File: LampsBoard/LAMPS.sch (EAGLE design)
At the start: 48 parts, among them IC1 LM358N, IC2 LM358N, IC3 5V, IC4 78L12Z, IC5 78L12Z, Q1 TIP120

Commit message: More work...
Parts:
- removed IC2: LM358N, linear:LM358N
- removed X, Y: (no value), pinhead:PINHD-1X1
- added 12V-AUX: (no value), SparkFun:M02PTH
- added 3.3V, 5V, VCC: (no value), adafruit:PINHD-1X1
- added ADCH1: 8-15, pinhead:PINHD-1X8
- added AUX1, COMM: 14-21, pinhead:PINHD-1X8
- added F3: MFR500, RepRapjr:PTCFUSE
- added IC6: UA741P, linear:UA741P
- added JP7: 22-37, pinhead:PINHD-2X8
- added R4, R5, R6, R7: 5K, SparkFun:RESISTORAXIAL-0.3
- added S2: (no value), switch-omron:31-XX
- added X-GALVO, Y-GALVO: 22-23-2031, con-molex:22-23-2031
- added X1: MSTBA2, con-phoenix-508:MSTBA2
- IC1: value LM358N -> UA741P; device linear:LM358N -> linear:UA741P
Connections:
- new net +12V: 12V-AUX.1, C10.1, C12.1, C13.1, F3.1, IC3.IN, IC4.VI, IC5.VI, Z-AXIS.VMOT
- new net N$27: IC6.V-, X-GALVO-3.S
- new net N$28: IC6.V+, X-GALVO-1.S
- new net N$29: COMM.2, COMMUNICATION.2
- new net N$30: R7.1
- new net N$31: IC1.OUT, R6.2, Y-GALVO-2.S
- new net N$32: IC1.V-, Y-GALVO-3.S
- new net N$33: IC1.V+, Y-GALVO-1.S
- new net N$34: IC1.+IN
- new net N$35: COMM.3, COMMUNICATION.3
- new net N$36: F3.2, X1-1.1
- new net N$37: COMM.4, COMMUNICATION.4
- new net N$38: COMM.5
- new net N$39: COMM.6, COMMUNICATION.6
- new net N$40: COMM.7, COMMUNICATION.7
- new net N$41: COMM.8, COMMUNICATION.8
- new net N$42: ADCH.1, ADCH1.1
- new net N$43: ADCH1.2
- new net N$44: ADCH.3, ADCH1.3
- new net N$45: ADCH.4, ADCH1.4
- new net N$46: ADCH.5, ADCH1.5
- new net N$47: ADCH.6, ADCH1.6
- new net N$48: ADCH.7, ADCH1.7
- new net N$49: ADCH.8, ADCH1.8
- new net N$50: JP1.15, JP7.15
- new net N$51: JP1.16, JP7.16
- new net N$52: JP1.13, JP7.13
- new net N$53: JP1.14, JP7.14
- new net N$54: JP1.11, JP7.11
- new net N$55: JP1.12, JP7.12
- new net N$56: JP1.9, JP7.9
- new net N$57: JP1.10, JP7.10
- new net N$58: JP1.7, JP7.7
- new net N$59: JP1.8, JP7.8
- new net N$60: JP1.5, JP7.5
- new net N$61: JP1.6, JP7.6
- new net N$62: JP1.3, JP7.3
- new net N$63: JP1.4, JP7.4
- new net N$64: JP1.1, JP7.1
- new net N$65: JP1.2, JP7.2
- new net N$74: AUX1.1, PWML.1
- new net N$75: AUX1.2, PWML.2
- new net N$76: AUX1.3, PWML.3
- new net N$77: AUX1.4, PWML.4
- new net N$78: AUX1.5, PWML.5
- new net N$79: AUX1.6, PWML.6
- new net N$80: AUX1.7, PWML.7
- new net RESET: POWER.1, S2.S
- net GND: now also 12V-AUX.2, AUX1.8, IC1.-IN, IC6.-IN, POWER.4, POWER.5, R4.1, R5.2, R6.1, R7.2, S2.P, X1-2.1
- net N$10: now also 5V.1, POWER.3; no longer IC2A.-IN, IC2A.OUT, Y.1
- net N$5: now also IC6.+IN; no longer IC1A.+IN
- net N$6: now also R5.1
- net N$7: now also IC6.OUT, R4.2, X-GALVO-2.S; no longer IC1A.-IN, IC1A.OUT, X.1
- net N$8: now also 3.3V.1, POWER.2; no longer AD420ARZ1.17, IC2A.+IN
- net N$9: now also COMM.1, COMMUNICATION.1; no longer AD420ARZ1.14, AD420ARZ1.15
- net VCC: now also VCC.1; no longer C10.1, C12.1, C13.1, IC3.IN, IC4.VI, IC5.VI, Z-AXIS.VMOT

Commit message: Switching AD420 Chip mount
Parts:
- removed AD420ARZ, AD420ARZ1: (no value), special:SW_DIP-12
- added AUX2: 14-21, pinhead:PINHD-1X8
- added B2, B3: (no value), SparkFun:M02PTH
- added IC2, IC7: AD420ARZ, ic-package:DIL24-3
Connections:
- new net D40: B3.1, JP2.14
- new net D42: B2.1, JP2.12
- new net N$66: AUX2.1, JP2.15
- new net N$67: AUX2.2, JP2.13
- new net N$68: AUX2.3, JP2.11
- new net N$69: AUX2.4, JP2.9
- new net N$70: AUX2.5, JP2.7
- new net N$71: AUX2.6, JP2.5
- new net N$72: AUX2.7, JP2.3
- new net N$73: AUX2.8, JP2.1
- net D10: now also IC7.9; no longer AD420ARZ.9
- net D11: now also IC2.7; no longer AD420ARZ1.7
- net D12: now also IC2.8; no longer AD420ARZ1.8
- net D7: now also IC2.9; no longer AD420ARZ1.9
- net D8: now also IC7.7; no longer AD420ARZ.7
- net D9: now also IC7.8; no longer AD420ARZ.8
- net GND: now also B2.2, B3.2, IC2.11, IC2.4, IC2.5, IC2.6, IC7.11, IC7.4, IC7.5, IC7.6; no longer AD420ARZ.11, AD420ARZ.4, AD420ARZ.5, AD420ARZ.6, AD420ARZ1.11, AD420ARZ1.4, AD420ARZ1.5, AD420ARZ1.6
- net N$1: now also IC2.21; no longer AD420ARZ1.21
- net N$18: now also IC7.23; no longer AD420ARZ.23
- net N$19: now also IC7.2; no longer AD420ARZ.2
- net N$2: now also IC2.20; no longer AD420ARZ1.20
- net N$24: now also IC2.2; no longer AD420ARZ1.2
- net N$25: now also IC2.23; no longer AD420ARZ1.23
- net N$3: now also IC7.21; no longer AD420ARZ.21
- net N$30: now also IC2.14, IC2.15
- net N$34: now also IC2.17
- net N$4: now also IC7.20; no longer AD420ARZ.20
- net N$5: now also IC7.17; no longer AD420ARZ.17
- net N$6: now also IC7.14, IC7.15; no longer AD420ARZ.14, AD420ARZ.15

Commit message: movin
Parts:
- removed JP7: 22-37, pinhead:PINHD-2X8
- IC2, IC7: value AD420ARZ -> (none); device ic-package:DIL24-3 -> ic-package:DIL24-6
- renumbered X1 to 12V
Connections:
- removed net N$50: JP1.15, JP7.15
- removed net N$51: JP1.16, JP7.16
- removed net N$52: JP1.13, JP7.13
- removed net N$53: JP1.14, JP7.14
- removed net N$54: JP1.11, JP7.11
- removed net N$55: JP1.12, JP7.12
- removed net N$56: JP1.9, JP7.9
- removed net N$57: JP1.10, JP7.10
- removed net N$58: JP1.7, JP7.7
- removed net N$59: JP1.8, JP7.8
- removed net N$60: JP1.5, JP7.5
- removed net N$61: JP1.6, JP7.6
- removed net N$62: JP1.3, JP7.3
- removed net N$63: JP1.4, JP7.4
- removed net N$64: JP1.1, JP7.1
- removed net N$65: JP1.2, JP7.2
- net N$38: now also COMMUNICATION.5
- net N$43: now also ADCH.2
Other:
- moved on the sheet: AUX1, COMMUNICATION

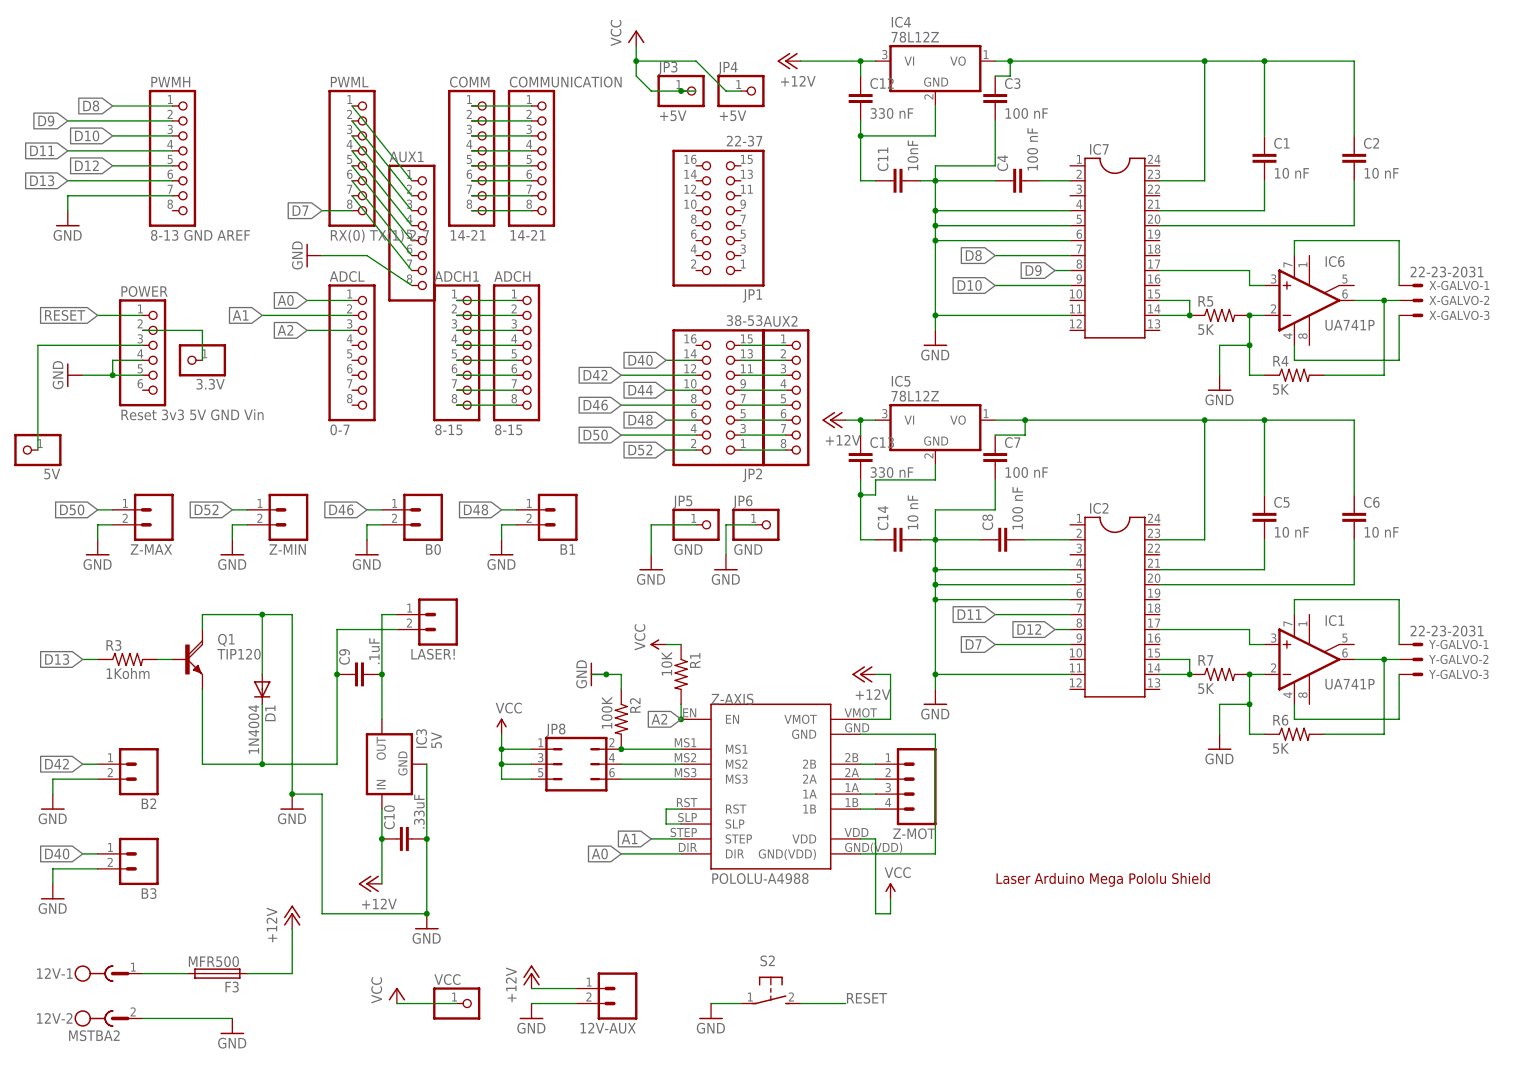
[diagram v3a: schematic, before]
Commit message: Remove expensive component for DIY variety
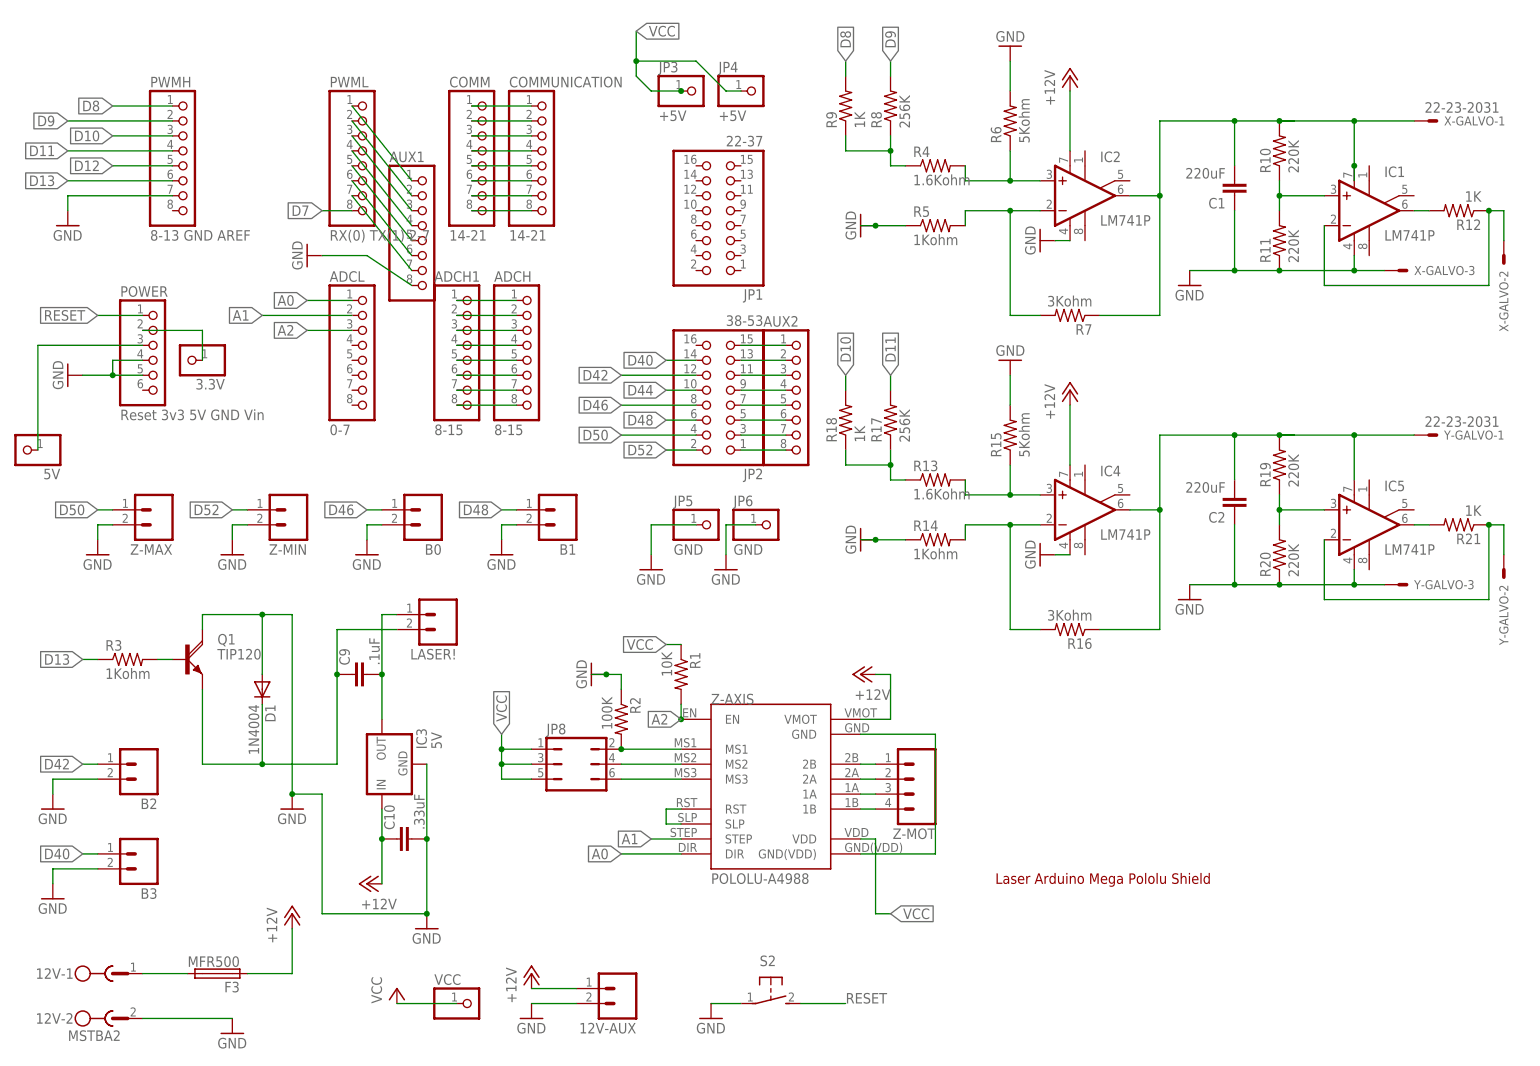
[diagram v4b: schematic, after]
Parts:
- removed C11: 10nF, capacitor-wima:C2,5-3
- removed C12, C13: 330 nF, capacitor-wima:C2,5-3
- removed C14, C5, C6: 10 nF, capacitor-wima:C2,5-3
- removed C3, C4, C7, C8: 100 nF, capacitor-wima:C2,5-3
- removed IC6: UA741P, linear:UA741P
- removed IC7: (no value), ic-package:DIL24-6
- added R10, R11, R19, R20: 220K, SparkFun:RESISTORAXIAL-0.3
- added R12, R18, R21, R9: 1K, SparkFun:RESISTORAXIAL-0.3
- added R13: 1.6Kohm, SparkFun:RESISTORAXIAL-0.3
- added R14: 1Kohm, SparkFun:RESISTORAXIAL-0.3
- added R15: 5Kohm, SparkFun:RESISTORAXIAL-0.3
- added R16: 3Kohm, SparkFun:RESISTORAXIAL-0.3
- added R17, R8: 256K, SparkFun:RESISTORAXIAL-0.3
- C1, C2: value 10 nF -> 220uF; device capacitor-wima:C2,5-3 -> SparkFun:CAPPTH
- IC1: value UA741P -> LM741P; device linear:UA741P -> linear:LM741P
- IC2: value (none) -> LM741P; device ic-package:DIL24-6 -> linear:LM741P
- IC4, IC5: value 78L12Z -> LM741P; device linear:78L12Z -> linear:LM741P
- R4: value 5K -> 1.6Kohm
- R5: value 5K -> 1Kohm
- R6: value 5K -> 5Kohm
- R7: value 5K -> 3Kohm
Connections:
- removed net N$30: IC2.14, IC2.15, R7.1
- removed net N$31: IC1.OUT, R6.2, Y-GALVO-2.S
- removed net N$32: IC1.V-, Y-GALVO-3.S
- removed net N$33: IC1.V+, Y-GALVO-1.S
- removed net N$34: IC1.+IN, IC2.17
- net +12V: now also IC2.V+, IC4.V+; no longer C12.1, C13.1, IC4.VI, IC5.VI
- net D10: now also R18.2; no longer IC7.9
- net D11: now also R17.2; no longer IC2.7
- net D12: no longer IC2.8
- net D7: no longer IC2.9
- net D8: now also R9.2; no longer IC7.7
- net D9: now also R8.2; no longer IC7.8
- net GND: now also C1.1, C2.1, IC1.V-, IC2.V-, IC4.V-, IC5.V-, R11.1, R14.1, R15.2, R20.1, R5.1, R6.2, X-GALVO-3.S, Y-GALVO-3.S; no longer C11.1, C11.2, C12.2, C14.2, C3.2, C4.1, C7.2, C8.1, IC1.-IN, IC2.11, IC2.4, IC2.5, IC2.6, IC4.GND, IC6.-IN, IC7.11, IC7.4, IC7.5, IC7.6, R4.1, R5.2, R6.1, R7.2
- net N$1: now also IC2.+IN, R4.2, R6.1; no longer C5.2, IC2.21
- net N$18: now also IC1.-IN, R12.1, X-GALVO-2.S; no longer C1.1, C2.1, C3.1, IC4.VO, IC7.23
- net N$19: now also IC4.-IN, R14.2, R16.2; no longer C4.2, IC7.2
- net N$2: now also IC2.-IN, R5.2, R7.2; no longer C6.2, IC2.20
- net N$24: now also R13.1, R17.1, R18.1; no longer C8.2, IC2.2
- net N$25: now also C2.2, IC4.OUT, IC5.V+, R16.1, R19.2, Y-GALVO-1.S; no longer C5.1, C6.1, C7.1, IC2.23, IC5.VO
- net N$26: now also IC5.+IN, R19.1, R20.2; no longer C13.2, C14.1, IC5.GND
- net N$27: now also IC5.OUT, R21.2; no longer IC6.V-, X-GALVO-3.S
- net N$28: now also IC5.-IN, R21.1, Y-GALVO-2.S; no longer IC6.V+, X-GALVO-1.S
- net N$3: now also IC1.+IN, R10.1, R11.2; no longer C1.2, IC7.21
- net N$4: now also R4.1, R8.1, R9.1; no longer C2.2, IC7.20
- net N$5: now also IC4.+IN, R13.2, R15.1; no longer IC6.+IN, IC7.17
- net N$6: now also C1.2, IC1.V+, IC2.OUT, R10.2, R7.1, X-GALVO-1.S; no longer IC7.14, IC7.15, R5.1
- net N$7: now also IC1.OUT, R12.2; no longer IC6.OUT, R4.2, X-GALVO-2.S
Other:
- moved on the sheet: C1, C2, IC1, R4, R5, R6, R7, X-GALVO-1, X-GALVO-2, X-GALVO-3, Y-GALVO-1, Y-GALVO-2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

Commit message: Some pcb work... adding in new schematic
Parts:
- 12V: MF (none) -> FARNELL; MPN (none) -> 1757242; OC_NEWARK (none) -> 71C4161
- 12V-AUX, 3.3V, 5V, ADCH, ADCH1, ADCL, AUX1, AUX2, B0, B1, B2, B3, C10, C9, COMM, COMMUNICATION, D1, F3, IC1, IC2, IC3, IC4, IC5, JP1, JP2, JP3, JP4, JP5, JP6, JP8, LASER!, POWER, PWMH, PWML, Q1, R1, R10, R11, R12, R13, R14, R15, R16, R17, R18, R19, R2, R20, R21, R3, R4, R5, R6, R7, R8, R9, VCC, Z-AXIS, Z-MAX, Z-MIN, Z-MOT: OC_NEWARK (none) -> unknown
- C1, C2: MPN (none) -> 100PK220MEFC12.5X20; OC_NEWARK (none) -> 39T8339
- S2: MPN (none) -> B3F-3100; OC_NEWARK (none) -> unknown
- X-GALVO, Y-GALVO: MF (none) -> MOLEX; MPN (none) -> 22-23-2031; OC_NEWARK (none) -> 30C0862
